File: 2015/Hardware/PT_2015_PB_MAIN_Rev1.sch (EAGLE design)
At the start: 136 parts, among them Q1 Q_INA28, Q10 Q_INA28, Q11 Q_IRFS7437PbF, Q12 2N7002, Q13 Q_INA28, Q14 Q_IRFS7437PbF, Q15 Q_INA28, Q16 Q_IRFS7437PbF, Q17 Q_INA28, Q18 Q_IRFS7437PbF, Q19 Q_INA28, Q2 Q_INA28, Q20 Q_IRFS7437PbF, Q3 Q_INA28, Q4 Q_ACS711LC, Q5 Q_ACS711LC, Q6 Q_IRFS7437PbF, Q7 Q_IRFS7437PbF, Q8 Q_INA28, Q9 Q_IRFS7437PbF

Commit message: This is a literal sexual experience at this point
I'm going to need protection
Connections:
- net 12V-CRIT: now also Q5.IP+; no longer Q5.IP-
- net 5V-IMEAS: now also U$1.D6~/A7; no longer U$1.D8/A8
- net ARM_P-IMEAS: now also U$1.A4; no longer U$1.A5
- net AUX_P-IMEAS: now also U$1.A3; no longer U$1.A4
- net CRIT-IMEAS: now also U$1.D4/A6; no longer U$1.D6~/A7
- net M1-IMEAS: now also U$1.D8/A8; no longer U$1.D9~/A9
- net M2-IMEAS: now also U$1.D9~/A9; no longer U$1.D10~/A10
- net M3-IMEAS: now also U$1.D10~/A10; no longer U$1.A0
- net M4-IMEAS: now also U$1.A0; no longer U$1.A1
- net M5-IMEAS: now also U$1.A1; no longer U$1.A2
- net M6-IMEAS: now also U$1.A2; no longer U$1.A3
- net N$10: now also Q5.IP-; no longer Q5.IP+
- net PRIMARY-VMEAS: now also U$1.A5; no longer U$1.D4/A6
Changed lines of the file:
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@@
 <junction x="119.38" y="114.3"/>
 <wire x1="137.16" y1="121.92" x2="147.32" y2="121.92" width="0.1524" layer="91"/>
-<wire x1="147.32" y1="121.92" x2="147.32" y2="134.62" width="0.1524" layer="91"/>
-<wire x1="147.32" y1="134.62" x2="165.1" y2="134.62" width="0.1524" layer="91"/>
-<pinref part="Q5" gate="G$1" pin="IP+"/>
+<wire x1="147.32" y1="121.92" x2="147.32" y2="124.46" width="0.1524" layer="91"/>
 <pinref part="C9" gate="G$1" pin="1"/>
 <wire x1="127" y1="119.38" x2="127" y2="121.92" width="0.1524" layer="91"/>
@@
 <wire x1="127" y1="121.92" x2="137.16" y2="121.92" width="0.1524" layer="91"/>
 <wire x1="137.16" y1="121.92" x2="137.16" y2="119.38" width="0.1524" layer="91"/>
+<pinref part="Q5" gate="G$1" pin="IP-"/>
+<wire x1="165.1" y1="124.46" x2="147.32" y2="124.46" width="0.1524" layer="91"/>
 </segment>
 </net>
@@
 </segment>
 <segment>
-<pinref part="U$1" gate="G$1" pin="D4/A6"/>
-<wire x1="-215.9" y1="-48.26" x2="-226.06" y2="-48.26" width="0.1524" layer="91"/>
-<label x="-226.06" y="-48.26" size="1.27" layer="95" rot="R180" xref="yes"/>
+<pinref part="U$1" gate="G$1" pin="A5"/>
+<wire x1="-175.26" y1="-114.3" x2="-162.56" y2="-114.3" width="0.1524" layer="91"/>
+<label x="-162.56" y="-114.3" size="1.27" layer="95" xref="yes"/>
 </segment>
 </net>
@@
 </segment>
 <segment>
-<pinref part="U$1" gate="G$1" pin="D10~/A10"/>
-<wire x1="-175.26" y1="-68.58" x2="-162.56" y2="-68.58" width="0.1524" layer="91"/>
-<label x="-162.56" y="-68.58" size="1.27" layer="95" xref="yes"/>
+<pinref part="U$1" gate="G$1" pin="D9~/A9"/>
+<wire x1="-175.26" y1="-63.5" x2="-162.56" y2="-63.5" width="0.1524" layer="91"/>
+<label x="-162.56" y="-63.5" size="1.27" layer="95" xref="yes"/>
 </segment>
 </net>
@@
 </segment>
 <segment>
-<pinref part="U$1" gate="G$1" pin="A0"/>
-<wire x1="-175.26" y1="-88.9" x2="-162.56" y2="-88.9" width="0.1524" layer="91"/>
-<label x="-162.56" y="-88.9" size="1.27" layer="95" xref="yes"/>
+<pinref part="U$1" gate="G$1" pin="D10~/A10"/>
+<wire x1="-175.26" y1="-68.58" x2="-162.56" y2="-68.58" width="0.1524" layer="91"/>
+<label x="-162.56" y="-68.58" size="1.27" layer="95" xref="yes"/>
 </segment>
 </net>
@@
 </segment>
 <segment>
-<pinref part="U$1" gate="G$1" pin="A1"/>
-<wire x1="-175.26" y1="-93.98" x2="-162.56" y2="-93.98" width="0.1524" layer="91"/>
-<label x="-162.56" y="-93.98" size="1.27" layer="95" xref="yes"/>
+<pinref part="U$1" gate="G$1" pin="A0"/>
+<wire x1="-175.26" y1="-88.9" x2="-162.56" y2="-88.9" width="0.1524" layer="91"/>
+<label x="-162.56" y="-88.9" size="1.27" layer="95" xref="yes"/>
 </segment>
 </net>
@@
 </segment>
 <segment>
-<pinref part="U$1" gate="G$1" pin="A2"/>
-<wire x1="-175.26" y1="-99.06" x2="-162.56" y2="-99.06" width="0.1524" layer="91"/>
-<label x="-162.56" y="-99.06" size="1.27" layer="95" xref="yes"/>
+<pinref part="U$1" gate="G$1" pin="A1"/>
+<wire x1="-175.26" y1="-93.98" x2="-162.56" y2="-93.98" width="0.1524" layer="91"/>
+<label x="-162.56" y="-93.98" size="1.27" layer="95" xref="yes"/>
 </segment>
 </net>
 <net name="M6-IMEAS" class="0">
-<segment>
-<pinref part="U$1" gate="G$1" pin="A3"/>
-<wire x1="-175.26" y1="-104.14" x2="-162.56" y2="-104.14" width="0.1524" layer="91"/>
-<label x="-162.56" y="-104.14" size="1.27" layer="95" xref="yes"/>
-</segment>
 <segment>
 <pinref part="Q15" gate="G$1" pin="OUT"/>
@@
 <label x="-167.64" y="248.92" size="1.27" layer="95" xref="yes"/>
 </segment>
+<segment>
+<pinref part="U$1" gate="G$1" pin="A2"/>
+<wire x1="-175.26" y1="-99.06" x2="-162.56" y2="-99.06" width="0.1524" layer="91"/>
+<label x="-162.56" y="-99.06" size="1.27" layer="95" xref="yes"/>
+</segment>
 </net>
 <net name="AUX_P-IMEAS" class="0">
@@
 </segment>
 <segment>
-<pinref part="U$1" gate="G$1" pin="A4"/>
-<wire x1="-175.26" y1="-109.22" x2="-162.56" y2="-109.22" width="0.1524" layer="91"/>
-<label x="-162.56" y="-109.22" size="1.27" layer="95" xref="yes"/>
+<pinref part="U$1" gate="G$1" pin="A3"/>
+<wire x1="-175.26" y1="-104.14" x2="-162.56" y2="-104.14" width="0.1524" layer="91"/>
+<label x="-162.56" y="-104.14" size="1.27" layer="95" xref="yes"/>
 </segment>
 </net>
@@
 </segment>
 <segment>
-<pinref part="U$1" gate="G$1" pin="A5"/>
-<wire x1="-175.26" y1="-114.3" x2="-162.56" y2="-114.3" width="0.1524" layer="91"/>
-<label x="-162.56" y="-114.3" size="1.27" layer="95" xref="yes"/>
+<pinref part="U$1" gate="G$1" pin="A4"/>
+<wire x1="-175.26" y1="-109.22" x2="-162.56" y2="-109.22" width="0.1524" layer="91"/>
+<label x="-162.56" y="-109.22" size="1.27" layer="95" xref="yes"/>
 </segment>
 </net>
@@
 </segment>
 <segment>
-<pinref part="U$1" gate="G$1" pin="D8/A8"/>
-<wire x1="-175.26" y1="-58.42" x2="-162.56" y2="-58.42" width="0.1524" layer="91"/>
-<label x="-162.56" y="-58.42" size="1.27" layer="95" xref="yes"/>
+<pinref part="U$1" gate="G$1" pin="D6~/A7"/>
+<wire x1="-175.26" y1="-53.34" x2="-162.56" y2="-53.34" width="0.1524" layer="91"/>
+<label x="-162.56" y="-53.34" size="1.27" layer="95" xref="yes"/>
 </segment>
 </net>
@@
 <net name="12V-CRIT" class="0">
 <segment>
-<pinref part="Q5" gate="G$1" pin="IP-"/>
-<wire x1="165.1" y1="124.46" x2="157.48" y2="124.46" width="0.1524" layer="91"/>
-<wire x1="157.48" y1="124.46" x2="157.48" y2="111.76" width="0.1524" layer="91"/>
+<wire x1="157.48" y1="134.62" x2="157.48" y2="111.76" width="0.1524" layer="91"/>
 <wire x1="157.48" y1="111.76" x2="177.8" y2="111.76" width="0.1524" layer="91"/>
 <pinref part="C8" gate="G$1" pin="1"/>
@@
 <wire x1="205.74" y1="129.54" x2="208.28" y2="129.54" width="0.1524" layer="91"/>
 <label x="261.62" y="111.76" size="1.27" layer="95" xref="yes"/>
+<pinref part="Q5" gate="G$1" pin="IP+"/>
+<wire x1="157.48" y1="134.62" x2="165.1" y2="134.62" width="0.1524" layer="91"/>
 </segment>
 <segment>
@@
 </segment>
 <segment>
-<pinref part="U$1" gate="G$1" pin="D6~/A7"/>
-<wire x1="-175.26" y1="-53.34" x2="-162.56" y2="-53.34" width="0.1524" layer="91"/>
-<label x="-162.56" y="-53.34" size="1.27" layer="95" xref="yes"/>
+<pinref part="U$1" gate="G$1" pin="D4/A6"/>
+<wire x1="-215.9" y1="-48.26" x2="-226.06" y2="-48.26" width="0.1524" layer="91"/>
+<label x="-226.06" y="-48.26" size="1.27" layer="95" rot="R180" xref="yes"/>
 </segment>
 </net>
@@
 </segment>
 <segment>
-<pinref part="U$1" gate="G$1" pin="D9~/A9"/>
-<wire x1="-175.26" y1="-63.5" x2="-162.56" y2="-63.5" width="0.1524" layer="91"/>
-<label x="-162.56" y="-63.5" size="1.27" layer="95" xref="yes"/>
-</segment>
-</net>
+<pinref part="U$1" gate="G$1" pin="D8/A8"/>
+<wire x1="-175.26" y1="-58.42" x2="-162.56" y2="-58.42" width="0.1524" layer="91"/>
+<label x="-162.56" y="-58.42" size="1.27" layer="95" xref="yes"/>
+</segment>
+</net>

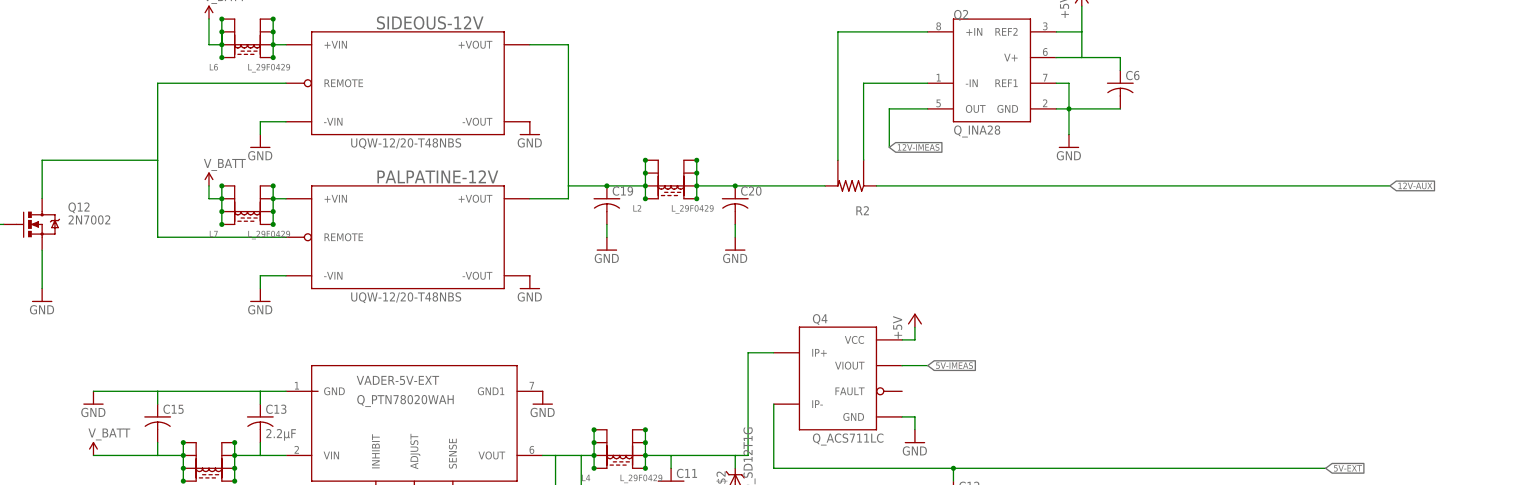
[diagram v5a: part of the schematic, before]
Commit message: Initial Powerboard Layout Completed.
Board layout finished. Passed DRC with zero airwires and 51 approved
errors (GND via overlap with SMD pads). One single ground plane cut was
used. Board will be rerouted for smaller size.
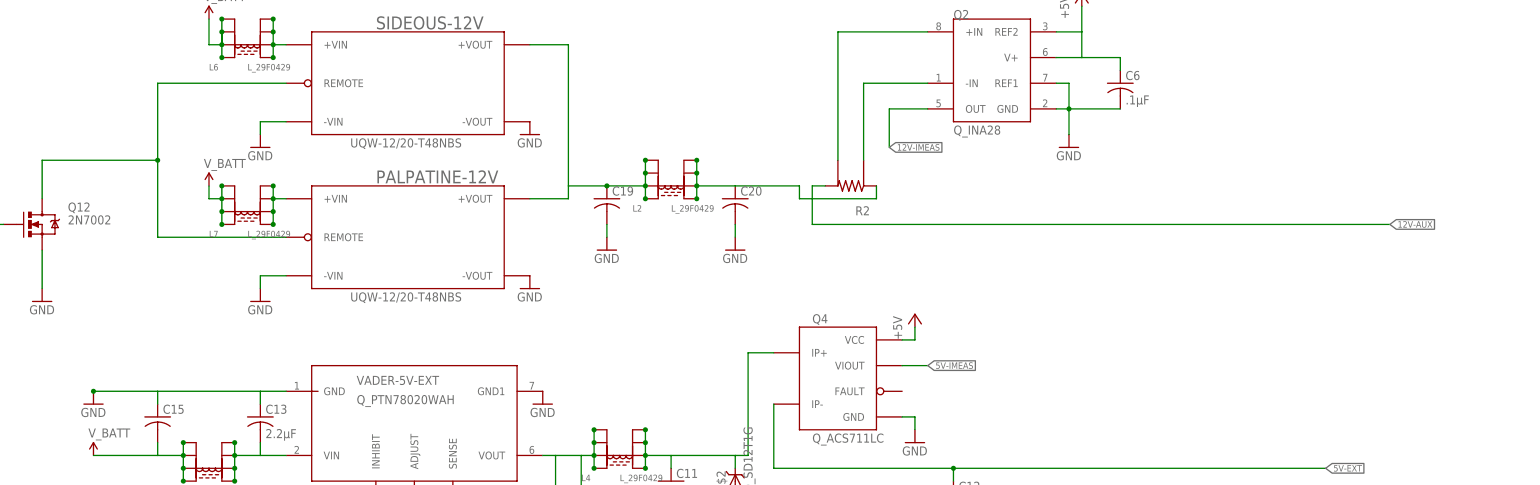
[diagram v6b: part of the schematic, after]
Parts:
- C6: value (none) -> .1µF
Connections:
- net 12V-AUX: now also R2.2; no longer R2.1
- net N$11: now also R2.1; no longer R2.2
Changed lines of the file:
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@@
 <part name="Q2" library="MRDT-2014-All" deviceset="Q_INA28" device=""/>
 <part name="GND7" library="SparkFun-Aesthetics" deviceset="GND" device=""/>
-<part name="C6" library="resistor" deviceset="C-US" device="C1206"/>
+<part name="C6" library="resistor" deviceset="C-US" device="C1206" value=".1µF"/>
 <part name="P+4" library="supply1" deviceset="+5V" device=""/>
 <part name="U$2" library="MRDT-2014-All" deviceset="D_SD12T1G" device=""/>
@@
 <pinref part="C15" gate="G$1" pin="1"/>
 <wire x1="15.24" y1="10.16" x2="15.24" y2="12.7" width="0.1524" layer="91"/>
+<junction x="2.54" y="12.7"/>
 </segment>
 <segment>
@@
 <pinref part="Q12" gate="G$1" pin="D"/>
 <wire x1="15.24" y1="58.42" x2="-7.62" y2="58.42" width="0.1524" layer="91"/>
+<junction x="15.24" y="58.42"/>
 </segment>
 </net>
@@
 <wire x1="121.92" y1="55.88" x2="121.92" y2="53.34" width="0.1524" layer="91"/>
 <wire x1="121.92" y1="53.34" x2="121.92" y2="50.8" width="0.1524" layer="91"/>
-<pinref part="R2" gate="G$1" pin="2"/>
-<wire x1="147.32" y1="53.34" x2="129.54" y2="53.34" width="0.1524" layer="91"/>
 <junction x="121.92" y="58.42"/>
 <pinref part="L2" gate="G$1" pin="7"/>
@@
 <pinref part="C20" gate="G$1" pin="1"/>
 <wire x1="129.54" y1="53.34" x2="121.92" y2="53.34" width="0.1524" layer="91"/>
-<junction x="129.54" y="53.34"/>
+<wire x1="129.54" y1="53.34" x2="142.24" y2="53.34" width="0.1524" layer="91"/>
+<wire x1="142.24" y1="53.34" x2="142.24" y2="50.8" width="0.1524" layer="91"/>
+<pinref part="R2" gate="G$1" pin="1"/>
+<wire x1="142.24" y1="50.8" x2="157.48" y2="50.8" width="0.1524" layer="91"/>
+<wire x1="157.48" y1="50.8" x2="157.48" y2="53.34" width="0.1524" layer="91"/>
 </segment>
 </net>
@@
 <net name="12V-AUX" class="0">
 <segment>
-<pinref part="R2" gate="G$1" pin="1"/>
-<wire x1="157.48" y1="53.34" x2="259.08" y2="53.34" width="0.1524" layer="91"/>
-<label x="259.08" y="53.34" size="1.27" layer="95" xref="yes"/>
-</segment>
-<segment>
+<wire x1="144.78" y1="45.72" x2="259.08" y2="45.72" width="0.1524" layer="91"/>
+<label x="259.08" y="45.72" size="1.27" layer="95" xref="yes"/>
+<pinref part="R2" gate="G$1" pin="2"/>
+<wire x1="147.32" y1="53.34" x2="144.78" y2="53.34" width="0.1524" layer="91"/>
+<wire x1="144.78" y1="53.34" x2="144.78" y2="45.72" width="0.1524" layer="91"/>
+</segment>
+<segment>
